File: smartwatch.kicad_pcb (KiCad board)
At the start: 2 copper layers, 34.4 x 215.2 mm, 104 parts, among them J1 505148-0408, J2 505147-0490, J3 505110-2491, J4 503480-0600, Q1 Si1308EDL, Q2 Si1308EDL, Q3 Si1308EDL, SW1 SKTDLDE010, SW2 SKTDLDE010, SW3 SKTDLDE010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

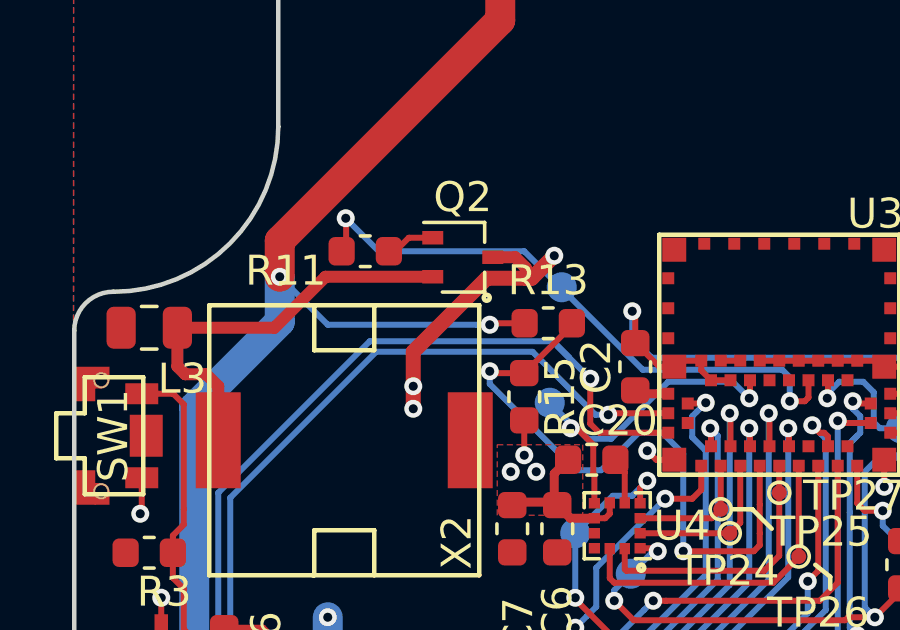
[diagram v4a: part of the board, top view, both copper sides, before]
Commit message: Fix: increase -BATT thickness for capacitor bank of display.
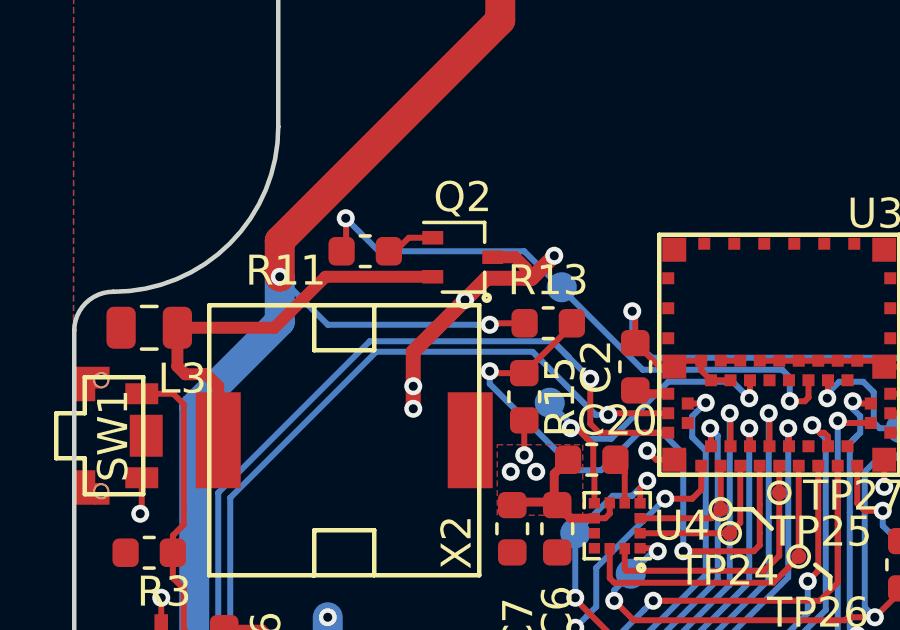
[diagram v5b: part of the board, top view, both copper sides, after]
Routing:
- net -BATT: vias 75 -> 76
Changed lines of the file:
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@@
     (thickness 1.6)
     (drawings 166)
-    (tracks 978)
+    (tracks 980)
     (zones 0)
     (modules 104)
@@
   (segment (start 96.05 124.25) (end 94.75 124.25) (width 0.5) (layer F.Cu) (net 2))
   (via (at 92.3 127.85) (size 0.6) (drill 0.3) (layers F.Cu B.Cu) (net 2))
-  (segment (start 94.75 124.25) (end 92.3 126.7) (width 0.5) (layer F.Cu) (net 2))
+  (segment (start 94.75 124.25) (end 94.025 124.975) (width 0.5) (layer F.Cu) (net 2))
   (segment (start 92.3 126.7) (end 92.3 127.85) (width 0.5) (layer F.Cu) (net 2))
   (via (at 92.3 128.6) (size 0.6) (drill 0.3) (layers F.Cu B.Cu) (net 2))
@@
   (segment (start 99.6 153.7) (end 100.375 153.7) (width 0.5) (layer F.Cu) (net 2))
   (via (at 99.6 153.7) (size 0.6) (drill 0.3) (layers F.Cu B.Cu) (net 2))
+  (segment (start 94.025 124.975) (end 92.3 126.7) (width 0.5) (layer F.Cu) (net 2))
+  (via (at 94.025 124.975) (size 0.6) (drill 0.3) (layers F.Cu B.Cu) (net 2))
   (via (at 101.6 156) (size 0.6) (drill 0.3) (layers F.Cu B.Cu) (net 3))
   (segment (start 101.6 154.7) (end 101.6 154.7) (width 0.5) (layer B.Cu) (net 3))

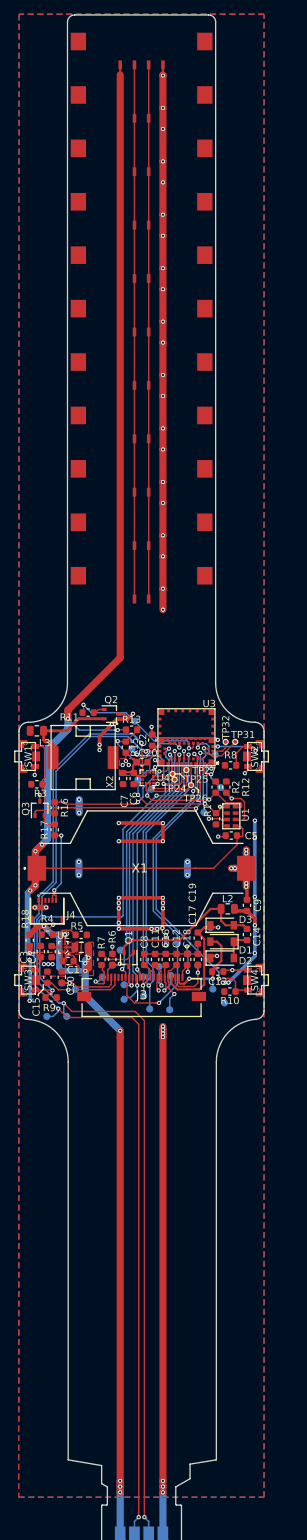
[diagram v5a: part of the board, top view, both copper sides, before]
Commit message: remove plane from wristband for better flexibility (OSHPark recommendation)
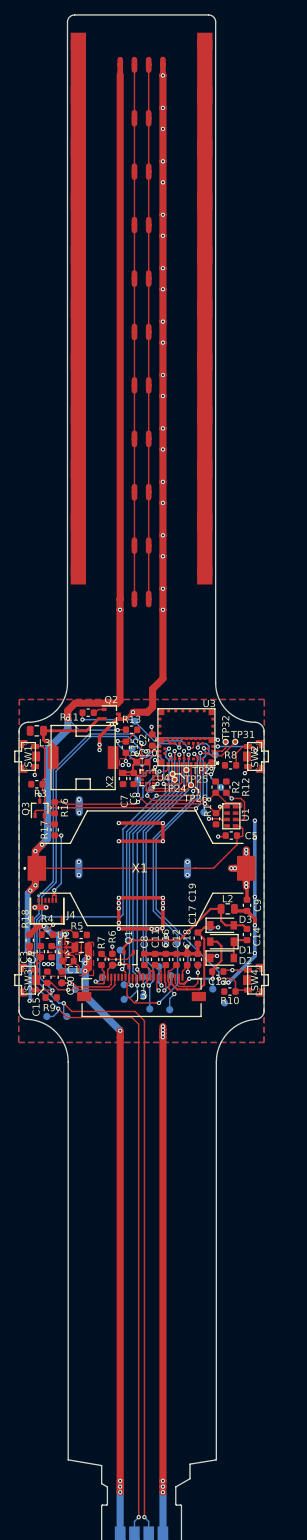
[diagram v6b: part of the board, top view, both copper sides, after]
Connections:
- J2 pad ~: +3V3 -> (no net) (x11)
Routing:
- net (no net): track 0.00 -> 150.0 mm
- net -BATT: track 265.9 -> 285.7 mm
- net +BATT: track 181.1 -> 185.3 mm, vias 7 -> 8
- net Net-(J2-Pad3): track 75.0 -> 76.5 mm
- net Net-(J2-Pad2): track 75.0 -> 76.5 mm
- net /BUZZER: track 20.2 -> 18.9 mm
